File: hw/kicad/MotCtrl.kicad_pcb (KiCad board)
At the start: 2 copper layers, 136 parts, among them P1 CONN_01X06, P2 CONN_01X03, P3 CONN_02X05, P4 CONN_01X05, Q1 FDBL0110N60, Q2 FDBL0110N60, Q3 FDBL0110N60, Q4 FDBL0110N60, Q5 FDBL0110N60, Q6 FDBL0110N60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

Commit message: More layout tryouts
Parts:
- moved Q3 24.7 mm to (212.3, 127.3)
- moved C28 16.8 mm to (196.8, 101.1), turned to 90 degrees
- moved R27 4.20 mm to (189.7, 127.2), turned to 180 degrees
- moved TP3 3.49 mm to (200.7, 105.9)
- moved C20 3.45 mm to (176.0, 113.3)
- moved C23 3.33 mm to (174.2, 112.8)
- moved R25 2.98 mm to (167.4, 113.3), turned to 180 degrees
- moved R28 2.67 mm to (188.7, 106.7), turned to 180 degrees
- moved Q6 2.58 mm to (172.7, 105.9)
- moved Q5 2.56 mm to (188.2, 105.9)
- moved C33 2.49 mm to (185.9, 114.8)
- moved U4 2.26 mm to (174.8, 114.6)
- moved R19 2.19 mm to (169.7, 113.3)
- moved R24 2.14 mm to (181.6, 113.3)
- moved C26 2.02 mm to (178.3, 115.1)
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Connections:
- R26 pad 1: Net-(C24-Pad1) -> /Power FET/MOT_PH_A
- R26 pad 2: /Power FET/MOT_PH_A -> Net-(C24-Pad1)
- R27 pad 1: Net-(C25-Pad1) -> /Power FET/MOT_PH_B
- R27 pad 2: /Power FET/MOT_PH_B -> Net-(C25-Pad1)
- R28 pad 1: Net-(C26-Pad1) -> /Power FET/MOT_PH_C
- R28 pad 2: /Power FET/MOT_PH_C -> Net-(C26-Pad1)
- U5 pad 2: Net-(R26-Pad4) -> Net-(R26-Pad3)
- U5 pad 3: Net-(R26-Pad3) -> Net-(R26-Pad4)
- U6 pad 2: Net-(R27-Pad4) -> Net-(R27-Pad3)
- U6 pad 3: Net-(R27-Pad3) -> Net-(R27-Pad4)
- U7 pad 2: Net-(R28-Pad4) -> Net-(R28-Pad3)
- U7 pad 3: Net-(R28-Pad3) -> Net-(R28-Pad4)
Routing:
- net Net-(C26-Pad1): track 10.1 -> 129.7 mm, vias 0 -> 100
- net GND: track 12.3 -> 34.9 mm, vias 0 -> 8
- net +12V: track 0.00 -> 9.14 mm, vias 0 -> 2
- net Net-(R28-Pad3): track 10.5 -> 4.69 mm
- net Net-(R28-Pad4): track 10.5 -> 4.69 mm
- net +3V3: track 0.00 -> 5.76 mm
- net Net-(Q5-Pad1): track 4.39 -> 5.91 mm
- net Net-(Q6-Pad1): track 3.93 -> 5.42 mm
- net (no net): track 1.00 -> 0.00 mm
- added copper zone on B.Cu, net Net-(C26-Pad1)
- added copper zone on F.Cu, net Net-(C26-Pad1)
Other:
- copper layers 2 -> 4
- net class Default: clearance 0.2 -> 0.127
- rule trace_clearance: 0.2 -> 0.127
- rule trace_min: 0.2 -> 0.127
- rule via_min_drill: 0.3 -> 0.254
- rule via_min_size: 0.4 -> 0.4572

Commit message: Aligned first power draft
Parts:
- C24, C7, Q1, Q2, R14, R15, R20, R21, U2: moved to B.Cu
- U5: moved to F.Cu
- moved C30 134.7 mm to (191.5, 149.4), turned to 270 degrees
- moved C29 130.2 mm to (185.9, 150.4), turned to 270 degrees
- moved R21 119.4 mm to (167.4, 148.8), turned to 180 degrees
- moved C24 106.4 mm to (178.3, 150.6), turned to 90 degrees
- moved R20 105.5 mm to (181.6, 148.8), turned to 180 degrees
- moved U2 105.2 mm to (174.8, 150.1), turned to 270 degrees
- moved R14 104.8 mm to (181.6, 150.6), turned to 0 degrees
- moved R15 101.2 mm to (169.7, 148.8), turned to 180 degrees
- moved C18 101.2 mm to (176.0, 148.8), turned to 90 degrees
- moved C21 100.3 mm to (174.2, 148.3), turned to 90 degrees
- moved Q1 97.2 mm to (188.2, 141.5), turned to 90 degrees
- moved U5 95.0 mm to (188.7, 148.1)
- moved C7 92.7 mm to (207.5, 141.5)
- moved R26 92.2 mm to (188.7, 142.2), turned to 180 degrees
- moved Q2 91.9 mm to (172.7, 141.5), turned to 90 degrees
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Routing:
- net +12V: track 9.14 -> 18.2 mm, vias 2 -> 4
- net Net-(C26-Pad1): track 129.7 -> 128.9 mm

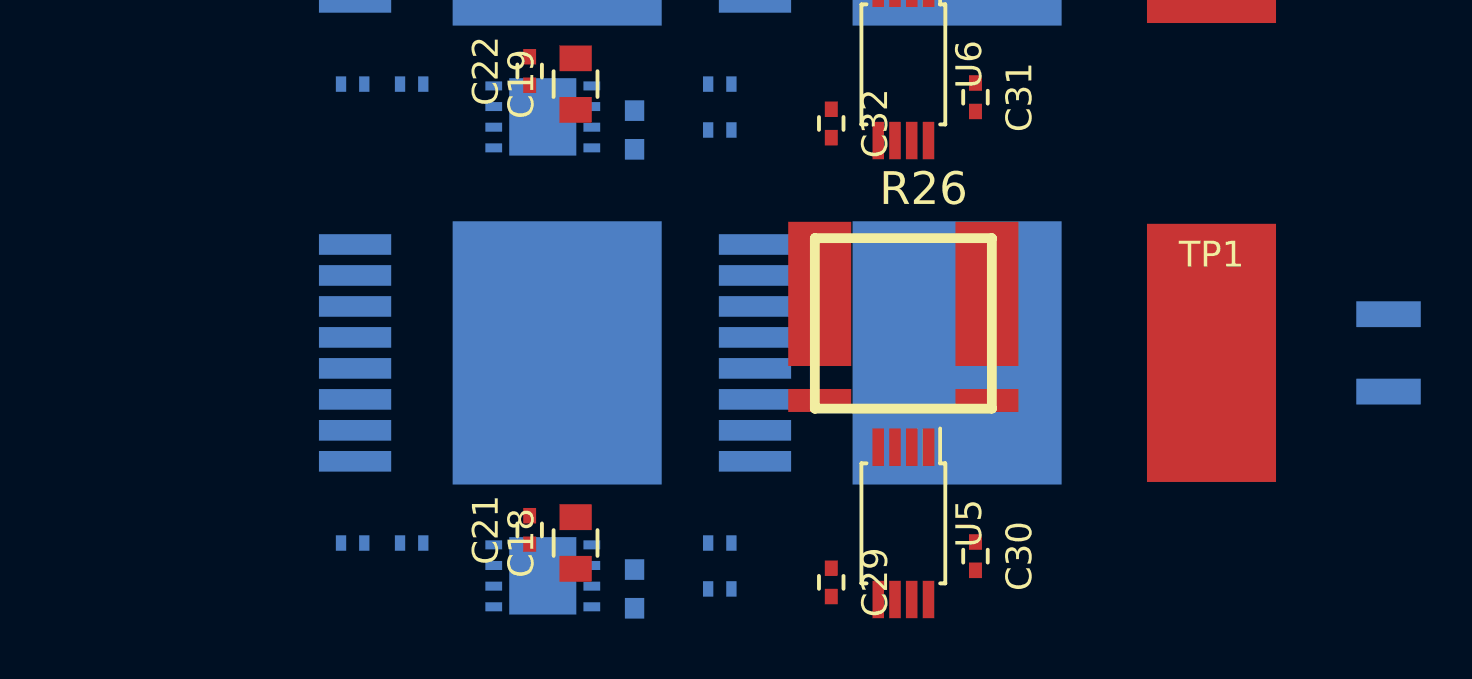
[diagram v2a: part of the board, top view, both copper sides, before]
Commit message: Alternative layout with smaller total vertical footprint
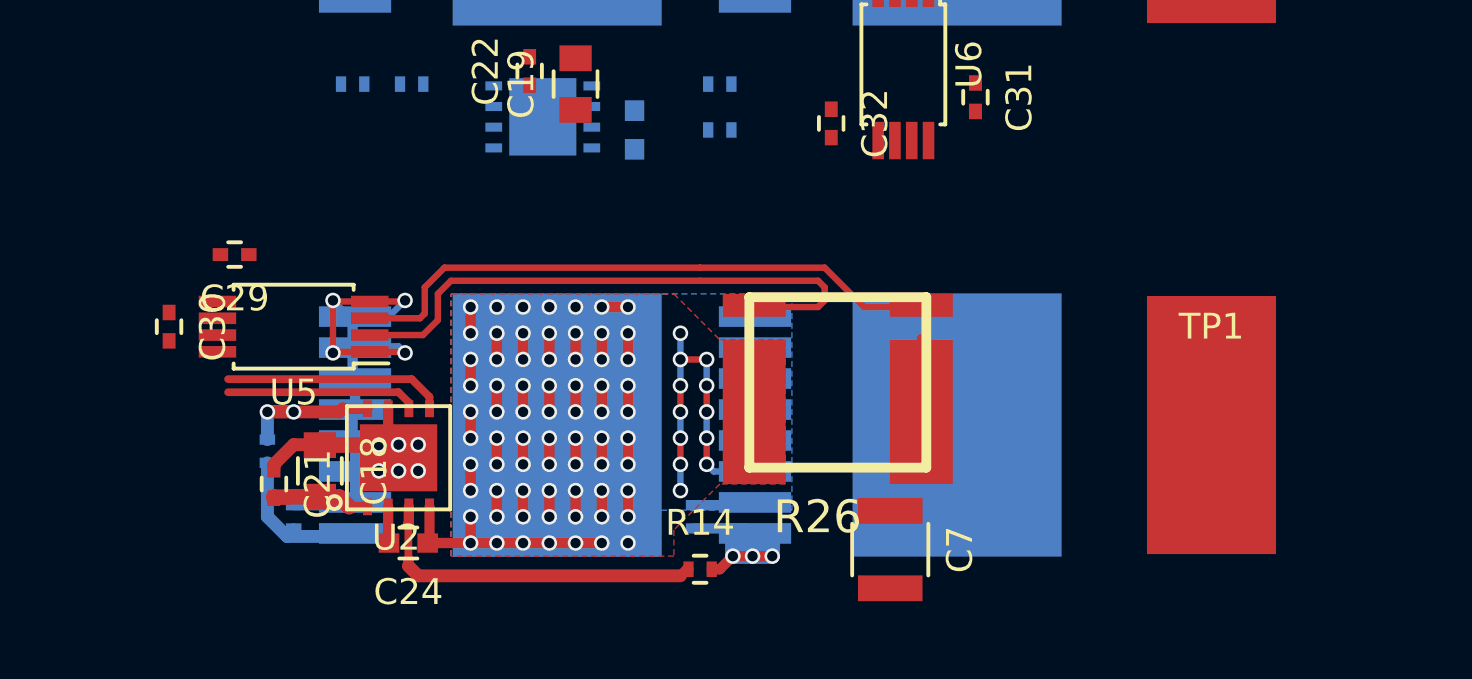
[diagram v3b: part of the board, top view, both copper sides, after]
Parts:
- C24, C7, R14, U2: moved to F.Cu
- moved C30 32.5 mm to (160.3, 140.5)
- moved C29 26.4 mm to (162.8, 137.7), turned to 180 degrees
- moved U5 24.8 mm to (165.1, 140.5), turned to 180 degrees
- moved C7 20.8 mm to (188.2, 149.1), turned to 270 degrees
- moved C18 10.3 mm to (166.1, 146.1), turned to 270 degrees
- moved C21 10.1 mm to (164.3, 146.6), turned to 270 degrees
- moved C24 8.94 mm to (169.5, 148.8), turned to 180 degrees
- moved U2 7.22 mm to (169.2, 145.5), turned to 0 degrees
- moved R15 6.62 mm to (164.1, 145.3), turned to 270 degrees
- moved R26 2.96 mm to (186.2, 140.7), turned to 0 degrees
- moved Q1 2.79 mm to (188.2, 144.3)
- moved Q2 2.79 mm to (172.7, 144.3)
- moved TP1 2.79 mm to (200.7, 144.3)
- moved R21 2.50 mm to (165.1, 147.8), turned to 90 degrees
- moved R20 1.44 mm to (180.6, 147.8), turned to 90 degrees
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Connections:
- R26 pad 1: /Power FET/MOT_PH_A -> Net-(C24-Pad1)
- R26 pad 2: Net-(C24-Pad1) -> /Power FET/MOT_PH_A
- R27 pad 1: /Power FET/MOT_PH_B -> Net-(C25-Pad1)
- R27 pad 2: Net-(C25-Pad1) -> /Power FET/MOT_PH_B
- R28 pad 1: /Power FET/MOT_PH_C -> Net-(C26-Pad1)
- R28 pad 2: Net-(C26-Pad1) -> /Power FET/MOT_PH_C
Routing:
- net Net-(C24-Pad1): track 0.00 -> 95.1 mm, vias 0 -> 82
- net GND: track 34.9 -> 73.9 mm, vias 8 -> 18
- net Net-(R26-Pad4): track 0.00 -> 23.8 mm
- net Net-(R26-Pad3): track 0.00 -> 22.8 mm
- net Net-(Q1-Pad1): track 0.00 -> 14.3 mm, vias 0 -> 3
- net Net-(R14-Pad1): track 0.00 -> 13.4 mm
- net /Microcontroller/PWM_H_A: track 0.00 -> 8.55 mm
- net /Microcontroller/PWM_L_A: track 0.00 -> 7.41 mm
- net Net-(Q2-Pad1): track 0.00 -> 6.28 mm
- net Net-(R15-Pad1): track 0.00 -> 6.02 mm, vias 0 -> 2
- net Net-(C26-Pad1): track 128.9 -> 125.0 mm
- net /Power FET/MOT_PH_C: track 0.00 -> 3.87 mm
- net +12V: track 18.2 -> 22.0 mm
- net Net-(C24-Pad2): track 0.00 -> 1.58 mm
- added copper zone on B.Cu, net Net-(C24-Pad1)
- added copper zone on F.Cu, net Net-(C24-Pad1)

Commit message: Yet another alternative
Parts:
- C25, R16, R17, U3: moved to F.Cu
- C32: moved to B.Cu
- moved C31 33.4 mm to (160.3, 119.9)
- moved C32 26.7 mm to (162.8, 119.1), turned to 180 degrees
- moved U6 25.8 mm to (165.1, 119.9), turned to 180 degrees
- moved C25 13.8 mm to (168.1, 123.4), turned to 270 degrees
- moved U3 13.0 mm to (164.8, 124.0), turned to 90 degrees
- moved C19 12.5 mm to (164.1, 127.3), turned to 0 degrees
- moved R17 9.94 mm to (161.3, 125.7), turned to 270 degrees
- moved C22 7.85 mm to (167.4, 126.7), turned to 180 degrees
- moved R23 6.76 mm to (161.8, 127.3), turned to 0 degrees
- moved R27 3.97 mm to (186.2, 121.4), turned to 0 degrees
- moved R22 3.94 mm to (180.6, 127.3), turned to 90 degrees
- moved R16 3.64 mm to (180.8, 129.3)
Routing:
- net GND: track 73.9 -> 125.5 mm, vias 18 -> 19
- net Net-(R27-Pad3): track 0.00 -> 22.6 mm
- net Net-(R27-Pad4): track 0.00 -> 22.5 mm
- net +12V: track 22.0 -> 42.4 mm, vias 4 -> 8
- net Net-(R16-Pad1): track 0.00 -> 18.9 mm
- net Net-(Q4-Pad1): track 0.00 -> 16.0 mm, vias 0 -> 4
- net Net-(Q3-Pad1): track 0.00 -> 12.5 mm, vias 0 -> 3
- net Net-(C25-Pad1): track 0.00 -> 5.74 mm
- net Net-(R17-Pad1): track 0.00 -> 1.74 mm
- net Net-(C25-Pad2): track 0.00 -> 1.47 mm

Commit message: work
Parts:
- added R43: 0R, Resistors_SMD:R_0402, F.Cu at (153.2, 123.4)
- C27, C32: moved to F.Cu
- C31: moved to B.Cu
- moved C27 21.8 mm to (187.2, 131.8), turned to 180 degrees
- moved C32 4.37 mm to (160.3, 122.7), turned to 270 degrees
- moved C31 2.87 mm to (162.3, 121.9), turned to 90 degrees
- moved Q3 2.79 mm to (188.2, 126.5)
- moved Q4 2.79 mm to (172.7, 126.5)
- moved R16 2.79 mm to (180.8, 132.1)
- moved TP2 2.79 mm to (200.7, 126.5)
- moved C19 2.79 mm to (164.1, 130.0)
- moved C22 2.79 mm to (167.4, 129.5)
- moved C25 2.79 mm to (168.1, 126.2)
- moved R17 2.79 mm to (161.3, 128.5)
- moved R22 2.79 mm to (180.6, 130.0)
- moved R23 2.79 mm to (161.8, 130.0)
- moved R27 2.79 mm to (186.2, 124.2)
- moved U3 2.79 mm to (164.8, 126.7)
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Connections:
- net Net-(C10-Pad1) renamed /Microcontroller/RST
- net Net-(C24-Pad1) renamed /Power FET/PH_A
- net Net-(C25-Pad1) renamed /Power FET/PH_B
- net Net-(C26-Pad1) renamed /Power FET/PH_C
- C30 pad 2: +3V3 -> /Power FET/I_SENSE_V_REF
- C32 pad 2: +3V3 -> /Power FET/I_SENSE_V_REF
- C34 pad 2: +3V3 -> /Power FET/I_SENSE_V_REF
- C9 pad 1: +3V3 -> /Power FET/I_SENSE_V_REF
- P4 pad 2: Net-(P4-Pad2) -> /Microcontroller/SWCLK
- P4 pad 4: Net-(P4-Pad4) -> /Microcontroller/SWDIO
- U1 pad 13: +3V3 -> /Power FET/I_SENSE_V_REF
- U1 pad 46: Net-(P4-Pad2) -> /Microcontroller/SWDIO
- U1 pad 49: Net-(P4-Pad4) -> /Microcontroller/SWCLK
- U5 pad 7: +3V3 -> /Power FET/I_SENSE_V_REF
- U6 pad 7: +3V3 -> /Power FET/I_SENSE_V_REF
- U7 pad 7: +3V3 -> /Power FET/I_SENSE_V_REF
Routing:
- net /Power FET/PH_B: track 5.74 -> 111.8 mm, vias 0 -> 85
- net GND: track 125.5 -> 181.0 mm, vias 19 -> 40
- net /Power FET/PH_C: track 125.0 -> 107.5 mm, vias 100 -> 83
- net /Power FET/MOT_PH_C: track 3.87 -> 21.4 mm, vias 0 -> 17
- net VPP: track 0.00 -> 14.5 mm, vias 0 -> 6
- net /Power FET/I_SENSE_V_REF: track 0.00 -> 3.80 mm
- net +3V3: track 5.76 -> 1.96 mm
- added copper zone on B.Cu, net /Power FET/PH_B
- added copper zone on F.Cu, net /Power FET/PH_B
- added copper zone on B.Cu, net Net-(C24-Pad1)
- added copper zone on F.Cu, net Net-(C24-Pad1)
- added copper zone on B.Cu, net Net-(C26-Pad1)
- added copper zone on F.Cu, net Net-(C26-Pad1)
- removed copper zone on B.Cu, net /Power FET/PH_A
- removed copper zone on F.Cu, net /Power FET/PH_A
- removed copper zone on B.Cu, net /Power FET/PH_C
- removed copper zone on F.Cu, net /Power FET/PH_C

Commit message: Go ahead with lower layout
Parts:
- C29: moved to B.Cu
- R15: moved to F.Cu
- moved R43 30.3 mm to (122.9, 121.9), turned to 270 degrees
- moved R21 3.78 mm to (161.5, 146.6)
- moved R15 2.40 mm to (162.1, 144.0), turned to 180 degrees
- moved C29 2.17 mm to (162.1, 139.7), turned to 90 degrees
- moved C18 1.80 mm to (164.3, 146.3)
- moved C24 1.80 mm to (167.8, 149.1)
- moved U2 1.80 mm to (167.4, 145.8)
- moved C21 1.78 mm to (162.6, 146.6)
- moved R26 1.27 mm to (186.2, 142.0)
- moved C7 1.14 mm to (187.2, 149.6), turned to 180 degrees
- moved R20 0.25 mm to (180.6, 148.1)
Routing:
- net GND: track 181.0 -> 262.1 mm, vias 40 -> 48
- net /Power FET/PH_A: track 95.1 -> 140.2 mm, vias 82 -> 85
- net VPP: track 14.5 -> 40.2 mm, vias 6 -> 12
- net +12V: track 42.4 -> 51.2 mm, vias 8 -> 12
- net Net-(Q1-Pad1): track 14.3 -> 7.88 mm
- net Net-(Q2-Pad1): track 6.28 -> 12.1 mm, vias 0 -> 4
- net Net-(R30-Pad1): track 0.00 -> 2.51 mm
- net Net-(R15-Pad1): track 6.02 -> 3.73 mm, vias 2 -> 0
- net +3V3: track 1.96 -> 3.95 mm, vias 0 -> 1
- net /Power FET/I_SENSE_V_REF: track 3.80 -> 5.80 mm
- net Net-(R14-Pad1): track 13.4 -> 15.1 mm
- net Net-(R26-Pad4): track 23.8 -> 22.5 mm
- net /Microcontroller/PWM_L_A: track 7.41 -> 8.57 mm
- net Net-(R26-Pad3): track 22.8 -> 21.7 mm
- net /Microcontroller/PWM_H_A: track 8.55 -> 9.56 mm
- added copper zone on F.Cu, net /Power FET/MOT_PH_A
- added copper zone on B.Cu, net /Power FET/PH_A
- added copper zone on F.Cu, net /Power FET/PH_A
- removed copper zone on B.Cu, net Net-(C24-Pad1)
- removed copper zone on F.Cu, net Net-(C24-Pad1)

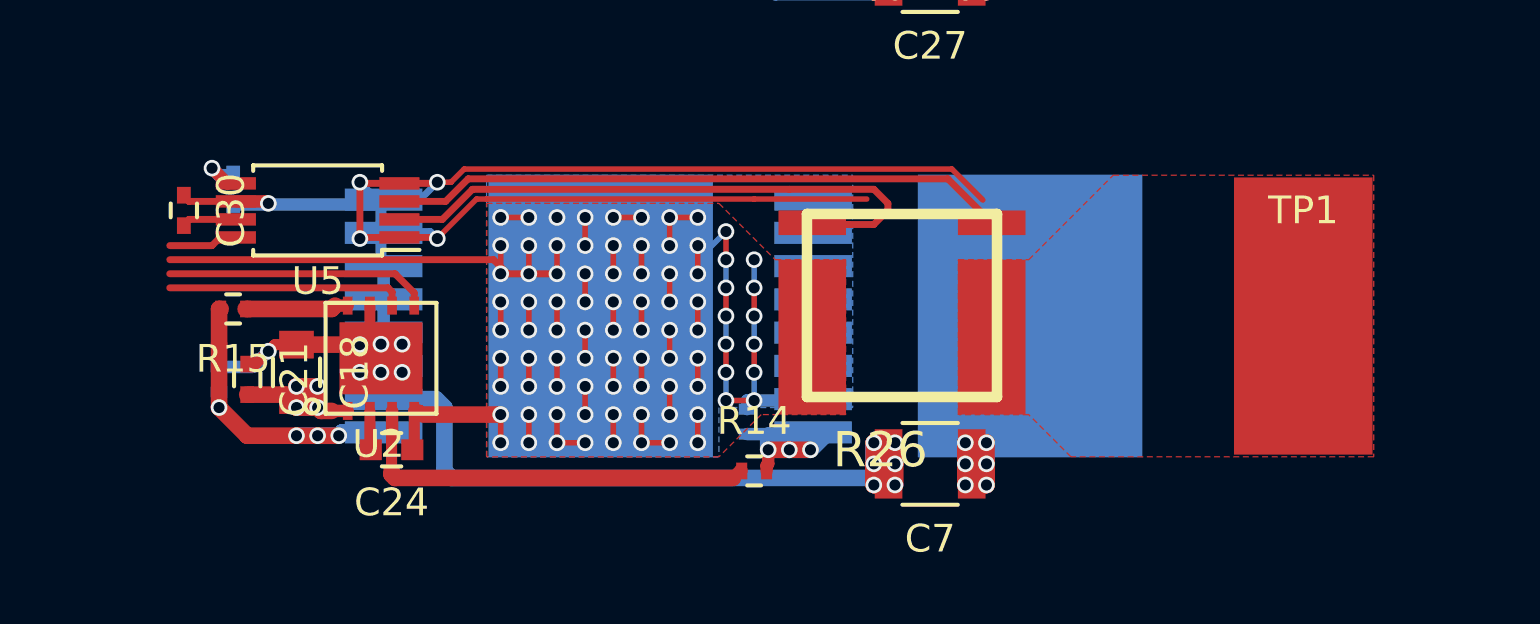
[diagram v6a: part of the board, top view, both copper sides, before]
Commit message: Som smaller fixes to lower layout
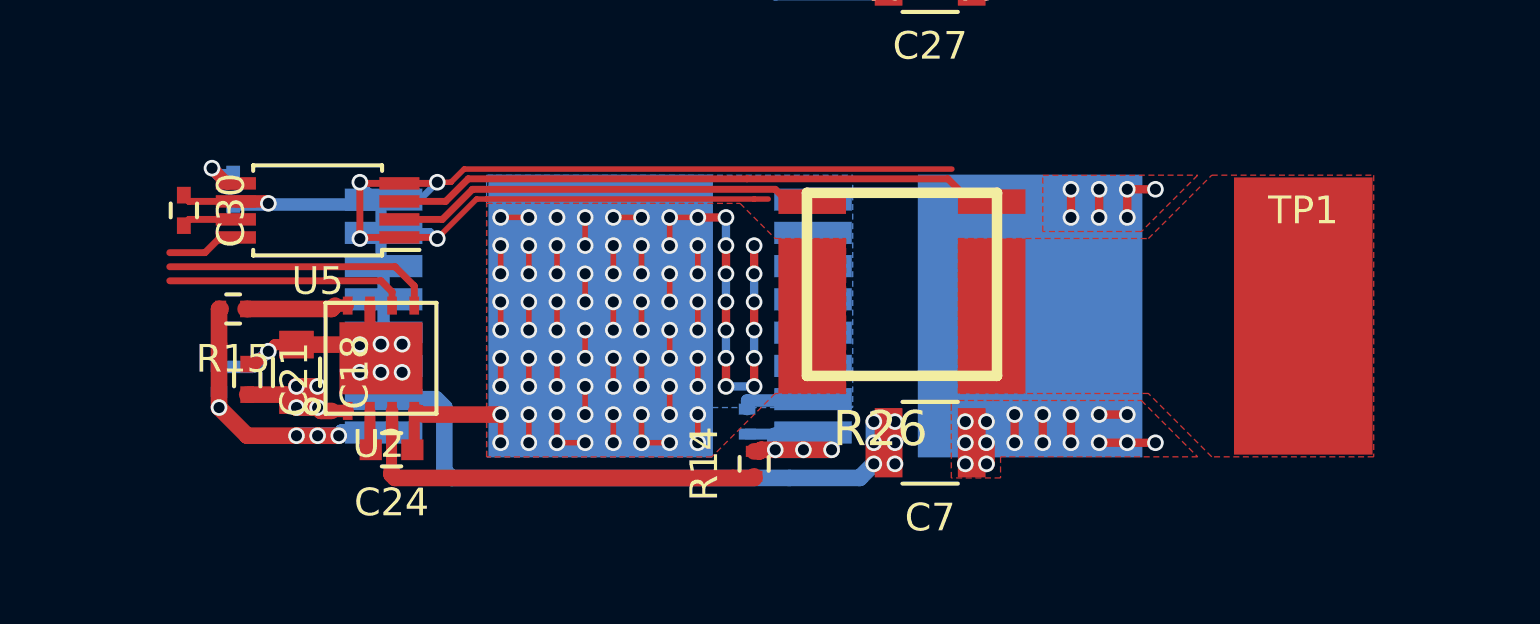
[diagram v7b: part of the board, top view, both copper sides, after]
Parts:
- moved C7 0.76 mm to (187.2, 148.8)
- moved R26 0.76 mm to (186.2, 141.2)
- moved R14 0.25 mm to (180.8, 149.6), turned to 90 degrees
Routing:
- net VPP: track 40.2 -> 62.6 mm, vias 12 -> 30
- net GND: track 262.1 -> 240.8 mm
- net /Power FET/PH_A: track 140.2 -> 122.7 mm
- net Net-(R26-Pad3): track 21.7 -> 15.5 mm
- net Net-(Q1-Pad1): track 7.88 -> 10.3 mm
- net Net-(R30-Pad1): track 2.51 -> 3.18 mm
- added copper zone on F.Cu, net VPP
